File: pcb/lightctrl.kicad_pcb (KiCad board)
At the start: 2 copper layers, 71.1 x 22.9 mm, 30 parts, among them IC1 ESP-WROOM-02, P1 LED_CONN, P2 PROG, P3 IO, P4 BATT_SENSE, P5 5V, Q1 BSS138, Q2 IRF8788, SW1 SW_FLASH, SW2 SW_RST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

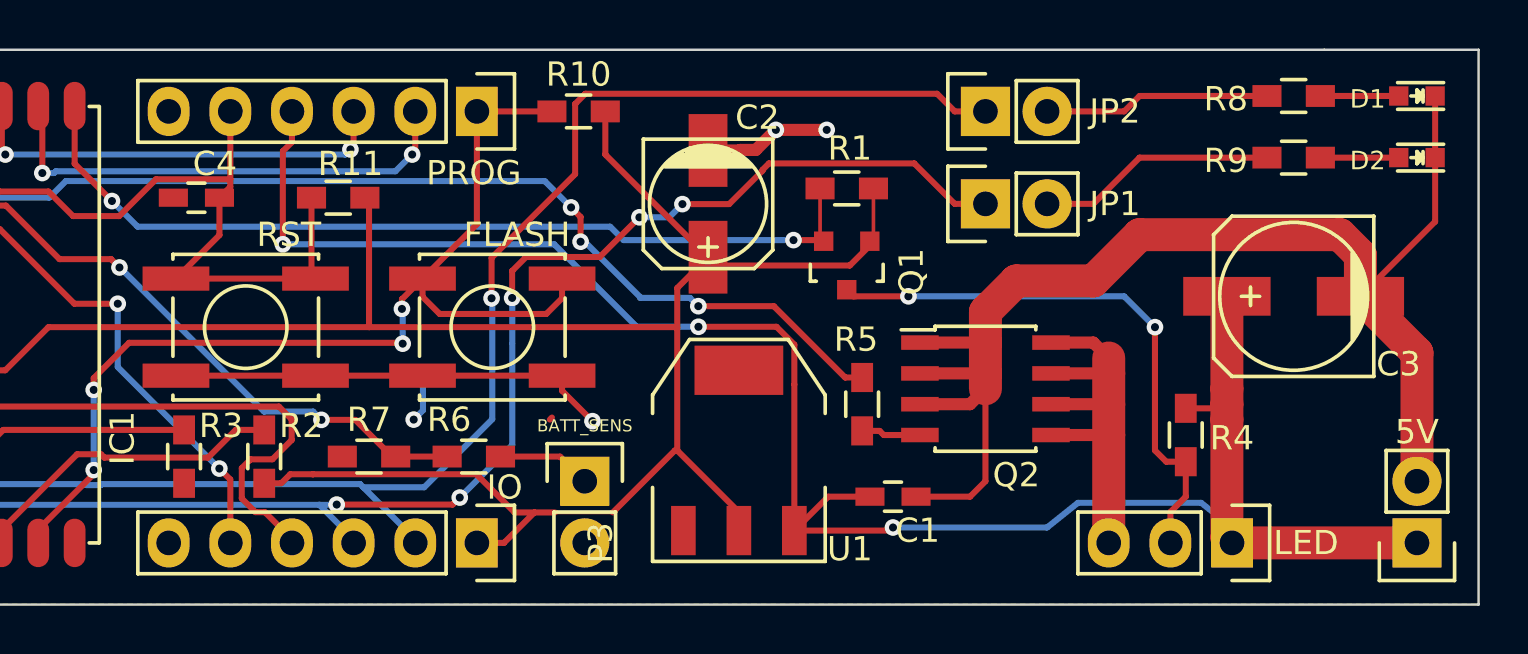
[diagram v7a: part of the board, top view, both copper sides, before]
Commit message: Pin header silkscreen, more ground vias
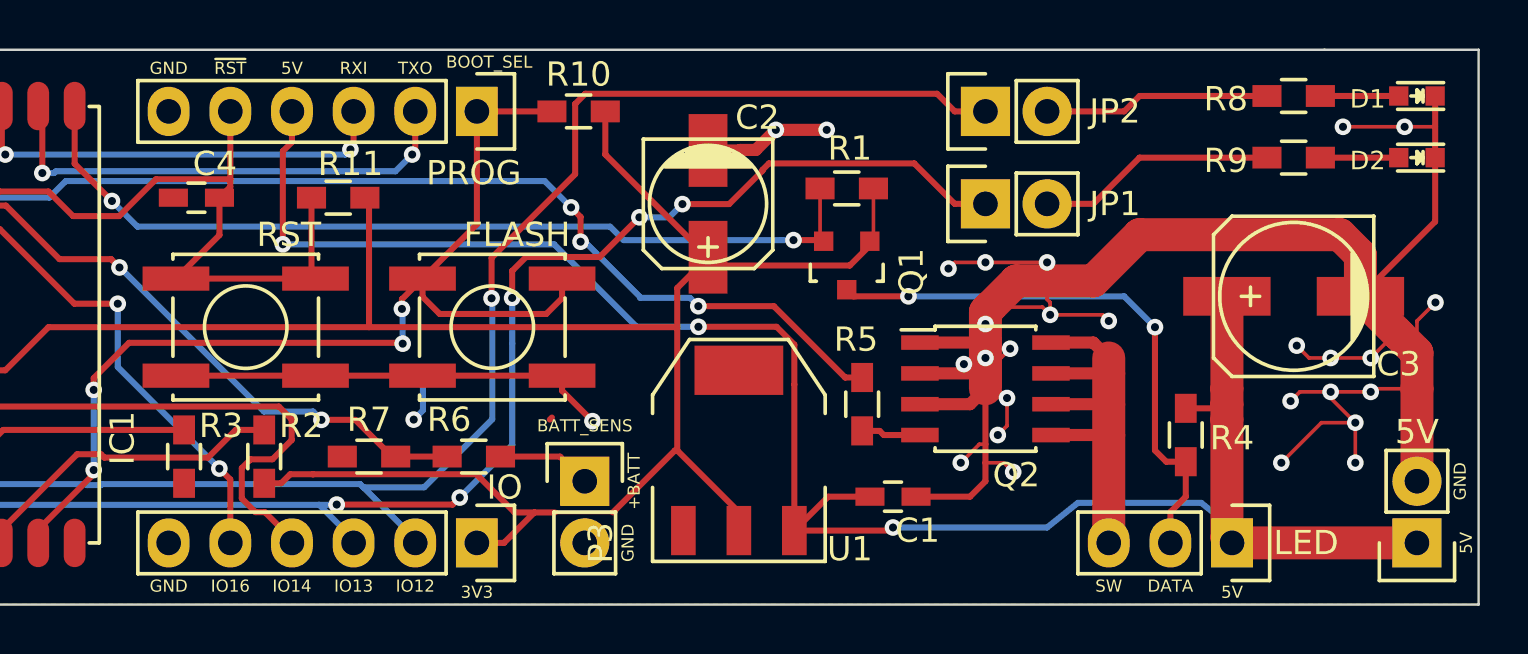
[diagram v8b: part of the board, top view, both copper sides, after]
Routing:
- net GND: track 78.9 -> 123.7 mm, vias 3 -> 28
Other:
- board text added: "+BATT"
- board text added: "3V3"
- board text added: "BOOT_SEL"
- board text added: "DATA"
- board text added: "GND"
- board text added: "IO12"
- board text added: "IO13"
- board text added: "IO14"
- board text added: "IO16"
- board text added: "RXI"
- board text added: "SW"
- board text added: "TXO"
- board text added: "~RST"
